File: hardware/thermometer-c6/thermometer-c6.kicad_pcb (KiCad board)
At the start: 2 copper layers, 48 x 35 mm, 101 parts, among them J1 JST-PH-2 BAT, J2 MEAS_HDR, J3 USB-C, J4 EPD FPC24 0.5mm, J5 DEBUG, Q1 AO3401A, Q2 AO3401A, Q3 Si1308EDL, Q4 AO3401A, Q5 2N7002, Q6 AO3401A, SW1 RESET, SW2 BOOT, U1 ESP32-C6-MINI-1-N4, U2 RT9080-33GJ5, U3 USBLC6-2SC6, U4 MCP73831-2, U5 BMP581, U6 BMP585, Y1 32.768kHz FC-135

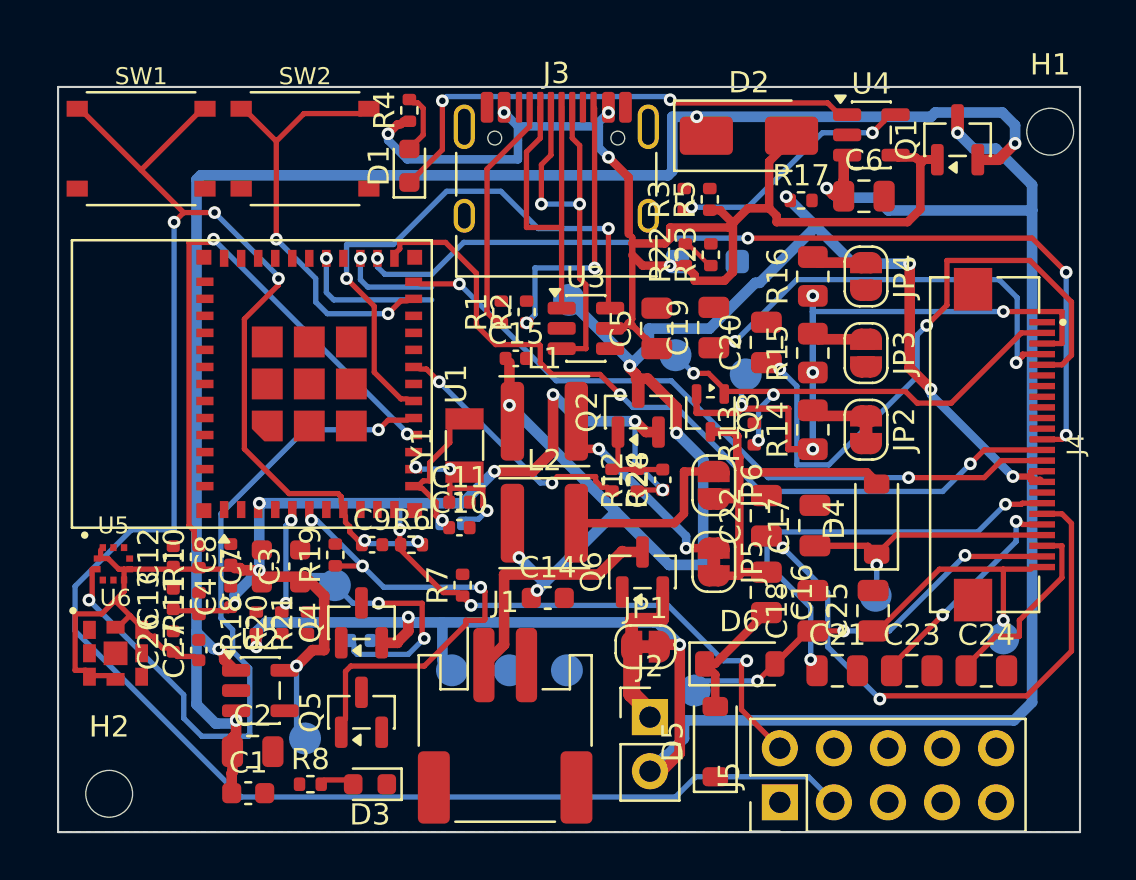
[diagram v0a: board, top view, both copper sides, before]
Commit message: Rebuild the divider block around its shared nodes; fence BOOT
R18/R20/R21 sat in one row at y25.17 with every shared node running
diagonally across it, and the row's north pads were 0.645mm from C3/C7's
(a 0.25mm lane needs 0.65). All four terminals starved.

Stack R20 over R21 instead, so VBAT_ADC is a 0.71mm link between adjacent
pads; R20 rot 180 puts ~VDIV_TOP straight across 1.77mm of clear copper
into Q4.3; R18 rot 270 drops ~VDIV_PGATE onto a lane under the ladder.
VBAT reaches R18.1 through a via-in-pad, so its 0.5mm B.Cu lane no longer
needs an F.Cu stub through the gate node's only escape. VBAT_ADC (50k
Thevenin) now runs 5mm to U1.5 through the C7/C3 pad channel instead of
the router's 15mm loop around the JST.

Box BOOT's A* to U1's north-east quadrant: with the divider unblocked it
reached R7.2 by running 60mm around the south edge and up the single
0.3mm B.Cu column between the antenna keep-out and the VSYS lane -- the
one corridor EN needs for SW1. R7.2 waits for R7 to move.

21 -> 17 unrouted terminals. DRC copper-clean.

Co-Authored-By: Claude Opus 4.8 (1M context) <noreply@anthropic.com>
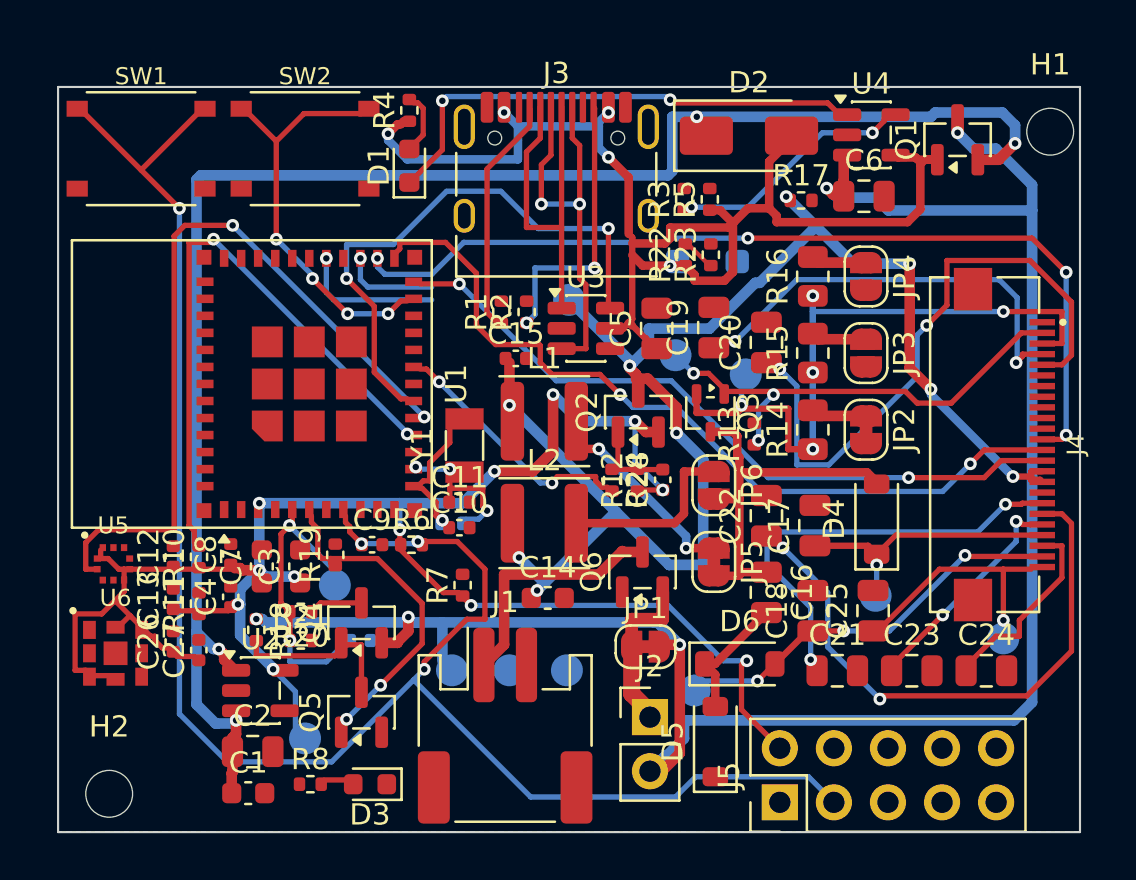
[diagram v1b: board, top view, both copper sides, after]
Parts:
- moved R20 1.03 mm to (111.4, 124.7), turned to 180 degrees
- moved R21 0.89 mm to (111.4, 126.0), turned to 0 degrees
- moved R18 0.33 mm to (109.3, 125.5), turned to -90 degrees
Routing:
- net EN: track 96.9 -> 84.6 mm, vias 5 -> 4
- net Net-(Q4-G): track 0.00 -> 8.36 mm
- net VDIV_EN: track 22.0 -> 14.9 mm, vias 3 -> 2
- net VBAT_ADC: track 17.1 -> 14.5 mm, vias 4 -> 2
- net Net-(Q4-D): track 0.00 -> 2.51 mm
- net SCL: track 34.1 -> 35.8 mm
- net +3V3: track 93.7 -> 92.0 mm, vias 11 -> 12
- net VBAT: track 96.0 -> 94.6 mm
- net BOOT: track 19.5 -> 18.9 mm, vias 2 -> 4

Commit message: Author J4's digital fan-out; route EPD_VCC before the signals
Pins 9..14 escape west at the connector's 0.5mm pitch and spread to 0.7mm,
the pitch a 0.6mm via needs beside a neighbouring lane. The six drops
cascade from the south, each in its own x-window: two parallel 45-degree
legs 0.5mm apart are only 0.354mm apart perpendicular, so no lane may be
diagonal beside a diagonal. The vias land in a staircase, not the usual
two columns -- each lane has to clear EPD_VCC's 45-degree B.Cu feed
(x-y = 26.55) before it can dive, and nothing here runs parallel to it.

EPD_VCC moves ahead of those six in ROUTE_PLAN. Q2.3's only escape is
north -- its own gate and source pads wall the south -- into the same B.Cu
channel over TP8 that the digital lanes cross the booster on. Routed after
them it lost Q2.3 and TP5.1 outright, and authoring around them cost four
HV escapes. Ordered first it takes a short F.Cu run through the y13.4
channel instead of the 20mm B.Cu loop it used to make.

Drop three pieces of authored copper the router now bypasses: EPD_CS and
EPD_DC's east-going stubs off U1's north row (both leave through their
via-in-pads instead, and the stubs walled the flank), EPD_DC's fan lane
(it escapes J4.11 eastward round the north edge) and EPD_SCK's staircase
via (it reaches the lane on F.Cu).

21 -> 15 unrouted terminals; EPD_MOSI/SCK/CS/DC and DBG_TX land. DRC
copper-clean; the remaining dangling copper is EPD_RST's and EPD_BUSY's,
and goes away when they route.

Co-Authored-By: Claude Opus 4.8 (1M context) <noreply@anthropic.com>
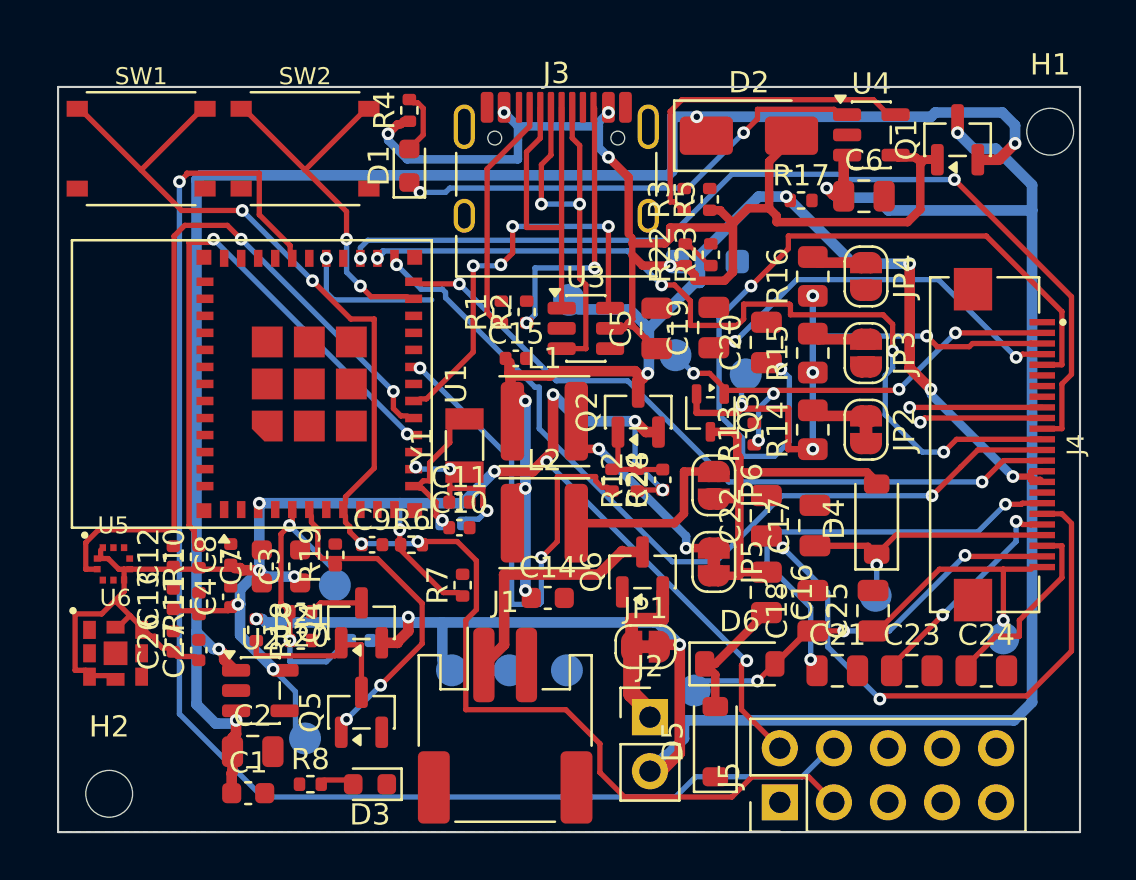
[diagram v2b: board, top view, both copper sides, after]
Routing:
- net DBG_TX: track 0.00 -> 65.9 mm, vias 0 -> 1
- net EPD_DC: track 4.49 -> 44.5 mm, vias 1 -> 2
- net EN: track 84.6 -> 65.2 mm
- net EPD_VCC: track 69.5 -> 55.4 mm, vias 9 -> 8
- net EPD_PWR_EN: track 11.5 -> 23.2 mm
- net USB_D-: track 26.2 -> 19.0 mm, vias 2 -> 4
- net Net-(J4-Pin_5): track 28.5 -> 35.6 mm
- net EPD_BUSY: track 6.69 -> 12.9 mm, vias 1 -> 2
- net EPD_RST: track 0.00 -> 5.81 mm, vias 0 -> 1
- net Net-(U4-PROG): track 11.0 -> 15.3 mm, vias 2 -> 0
- net EPD_RESE: track 30.3 -> 27.2 mm
- net BOOT: track 18.9 -> 16.4 mm, vias 4 -> 2
- net Net-(J4-Pin_4): track 19.2 -> 17.1 mm
- net EPD_SCK: track 37.7 -> 39.6 mm
- net EPD_CS: track 42.6 -> 40.8 mm
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
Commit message: Author J5's fan-in; keep the router's vias out of other holes
VBAT's 0.5mm B.Cu lane at y29.75 walls J5's entire north approach and
leaves 0.21mm of it clear of the pin rows. J5 is through-hole, so each
lane now surfaces on a via just north of that lane and drops onto the pads
on F.Cu, straight over it. The two outer-row pins come down the 0.84mm
channels between the inner pads, 0.295mm to each pad at 0.25mm width. The
five vias share one row at 1.27mm pitch.

route.py placed a via dead centre in J5.4's plated hole. build_bitmaps
stamps obstacles with *copper* clearance, and copper clearance is waived
against your own net -- so a same-net PTH pad reads as free space to drop a
via into. Hole-to-hole spacing has no such exemption. Stamp every drilled
pad and every via into the via bitmaps net-agnostically.

Still 15 unrouted, but the four debug lines and VBUS_SENSE now fail on
U1's side rather than J5's: the connector end is solved and the bus across
the board is what is left. DRC copper-clean. DBG_TX reaches J5.4 the long
way round the south edge for now, so its drop dangles until the bus lands.

Co-Authored-By: Claude Opus 4.8 (1M context) <noreply@anthropic.com>
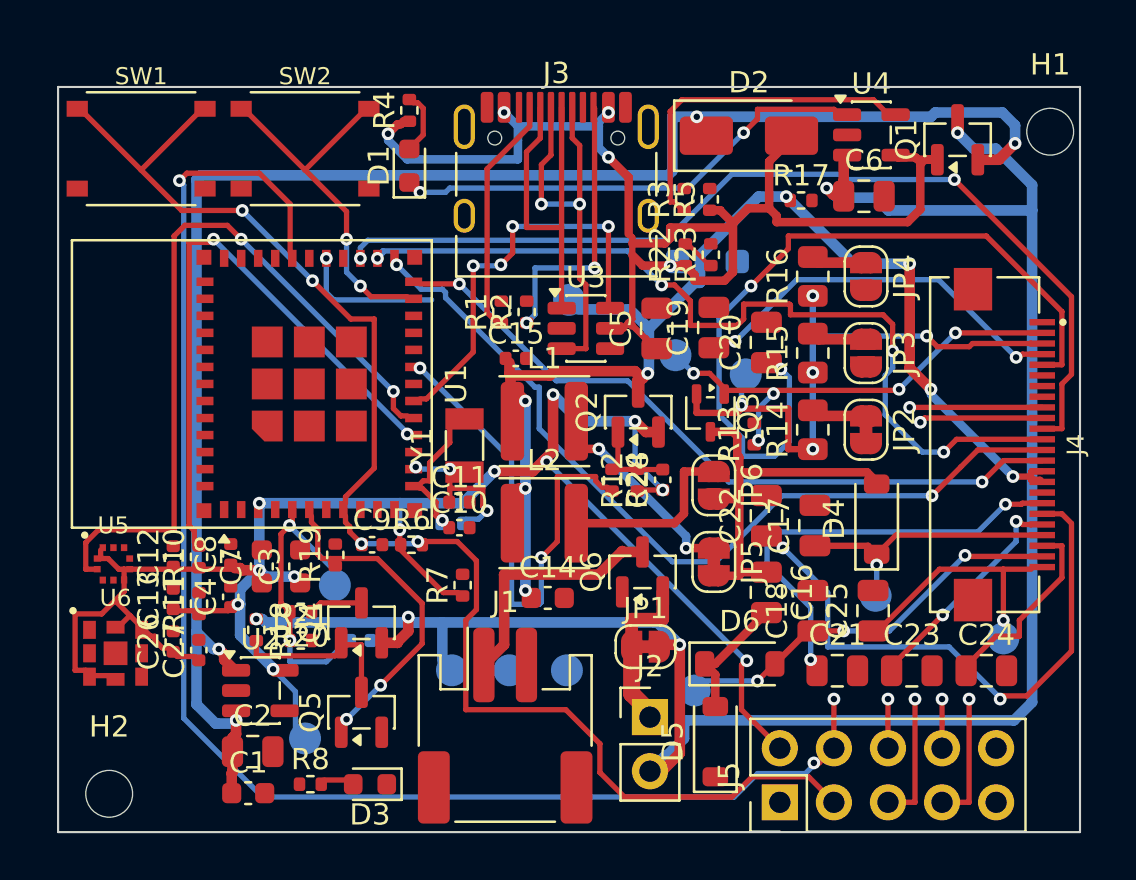
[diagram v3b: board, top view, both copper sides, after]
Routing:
- net DBG_RX: track 0.00 -> 6.12 mm, vias 0 -> 1
- net DBG_IO5: track 0.00 -> 6.12 mm, vias 0 -> 1
- net DBG_TX: track 65.9 -> 68.9 mm, vias 1 -> 3
- net VBUS_SENSE: track 1.79 -> 4.10 mm, vias 0 -> 1
- net DBG_IO8: track 0.00 -> 2.31 mm, vias 0 -> 1
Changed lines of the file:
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@@
 	)
 	(segment
-		(start 105.7 104.45)
-		(end 106.05 104.1)
+		(start 105.7 104.4)
+		(end 105.9 104.6)
 		(width 0.25)
-		(layer "F.Cu")
+		(layer "B.Cu")
 		(net "DBG_TX")
 	)
 	(segment
-		(start 105.7 129.449999)
-		(end 105.7 104.45)
+		(start 105.8 105.8)
+		(end 108.65 105.8)
 		(width 0.25)
-		(layer "B.Cu")
-		(net "DBG_TX")
+		(layer "F.Cu")
+		(net "EN")
 	)
 	(segment
-		(start 105.7 129.45)
-		(end 105.7 129.449999)
+		(start 105.9 104.6)
+		(end 105.9 129.65)
 		(width 0.25)
 		(layer "B.Cu")
@@
 	)
 	(segment
-		(start 105.8 105.8)
-		(end 108.65 105.8)
+		(start 105.9 129.65)
+		(end 109.6 133.35)
 		(width 0.25)
-		(layer "F.Cu")
-		(net "EN")
+		(layer "B.Cu")
+		(net "DBG_TX")
 	)
 	(segment
@@
 	(segment
 		(start 106.05 104.05)
-		(end 109.45 104.05)
-		(width 0.25)
-		(layer "F.Cu")
-		(net "DBG_TX")
-	)
-	(segment
-		(start 106.05 104.1)
-		(end 106.05 104.05)
+		(end 105.7 104.4)
 		(width 0.25)
 		(layer "F.Cu")
@@
 	(segment
 		(start 109.45 104.05)
-		(end 109.45 106)
-		(width 0.25)
-		(layer "F.Cu")
-		(net "DBG_TX")
-	)
-	(segment
-		(start 109.45 106)
-		(end 110.9 107.45)
+		(end 106.05 104.05)
 		(width 0.25)
 		(layer "F.Cu")
@@
 	(segment
 		(start 109.6 133.35)
-		(end 105.7 129.45)
+		(end 131.75 133.35)
 		(width 0.25)
 		(layer "B.Cu")
@@
 	)
 	(segment
-		(start 110.9 107.45)
-		(end 110.9 107.75)
+		(start 110.9 105.5)
+		(end 109.45 104.05)
+		(width 0.25)
+		(layer "F.Cu")
+		(net "DBG_TX")
+	)
+	(segment
+		(start 110.9 107.75)
+		(end 110.9 105.5)
 		(width 0.25)
 		(layer "F.Cu")
@@
 	)
 	(segment
-		(start 129 133.349999)
-		(end 129 133.35)
-		(width 0.25)
-		(layer "B.Cu")
-		(net "DBG_TX")
-	)
-	(segment
-		(start 129 133.35)
-		(end 109.6 133.35)
-		(width 0.25)
-		(layer "B.Cu")
-		(net "DBG_TX")
-	)
-	(segment
 		(start 129.199999 105.65)
 		(end 128.949999 105.4)
@@
 	)
 	(segment
-		(start 129.949999 132.4)
-		(end 129 133.349999)
-		(width 0.25)
-		(layer "B.Cu")
-		(net "DBG_TX")
-	)
-	(segment
 		(start 129.989999 114.4225)
 		(end 129.99 114.422501)
@@
 	)
 	(segment
+		(start 131.75 133.35)
+		(end 132.85 132.25)
+		(width 0.25)
+		(layer "B.Cu")
+		(net "DBG_TX")
+	)
+	(segment
 		(start 131.8 111.95)
 		(end 134.7 109.05)
@@
 	)
 	(segment
+		(start 132.85 132.25)
+		(end 135.1 132.25)
+		(width 0.25)
+		(layer "B.Cu")
+		(net "DBG_TX")
+	)
+	(segment
 		(start 132.9 105.15)
 		(end 134.199999 105.15)
@@
 	)
 	(segment
-		(start 134.95 132.4)
-		(end 129.949999 132.4)
+		(start 135.1 132.25)
+		(end 135.5 131.85)
 		(width 0.25)
 		(layer "B.Cu")
@@
 	)
 	(segment
+		(start 135.5 131.75)
+		(end 135.75 131.75)
+		(width 0.25)
+		(layer "F.Cu")
+		(net "DBG_TX")
+	)
+	(segment
+		(start 135.5 131.85)
+		(end 135.5 131.75)
+		(width 0.25)
+		(layer "B.Cu")
+		(net "DBG_TX")
+	)
+	(segment
 		(start 135.7125 108.25)
 		(end 137.95 108.25)
@@
 	)
 	(segment
-		(start 135.8 131.55)
-		(end 134.95 132.4)
-		(width 0.25)
-		(layer "B.Cu")
-		(net "DBG_TX")
-	)
-	(segment
-		(start 135.95 131.55)
-		(end 135.8 131.55)
+		(start 135.75 131.75)
+		(end 136.44 131.06)
 		(width 0.25)
-		(layer "B.Cu")
+		(layer "F.Cu")
 		(net "DBG_TX")
 	)
@@
 	(segment
 		(start 136.15 126.3)
-		(end 138.6 128.75)
+		(end 141.85 126.3)
 		(width 0.25)
 		(layer "B.Cu")
@@
 	)
 	(segment
+		(start 136.44 128.75)
+		(end 136.44 131.06)
+		(width 0.25)
+		(layer "F.Cu")
+		(net "DBG_TX")
+	)
+	(segment
+		(start 136.44 131.06)
+		(end 136.45 131.05)
+		(width 0.25)
+		(layer "F.Cu")
+		(net "DBG_TX")
+	)
+	(segment
 		(start 136.45 101.05)
 		(end 136.5 101.1)
@@
 	)
 	(segment
-		(start 138.6 128.75)
-		(end 138.75 128.6)
-		(width 0.25)
-		(layer "F.Cu")
-		(net "Net-(J4-Pin_19)")
-	)
-	(segment
 		(start 138.75 110.7)
 		(end 139.2 111.15)
@@
 	)
 	(segment
-		(start 138.75 128.6)
-		(end 145.5 128.6)
-		(width 0.25)
-		(layer "F.Cu")
-		(net "Net-(J4-Pin_19)")
-	)
-	(segment
 		(start 138.8 125.25)
 		(end 141.4 122.65)
@@
 	)
 	(segment
+		(start 138.98 128.75)
+		(end 138.98 131.06)
+		(width 0.25)
+		(layer "F.Cu")
+		(net "VBUS_SENSE")
+	)
+	(segment
 		(start 139 105.8)
 		(end 138.4 105.2)
@@
 	)
 	(segment
+		(start 140.25 128.75)
+		(end 140.25 133.6)
+		(width 0.25)
+		(layer "F.Cu")
+		(net "DBG_RX")
+	)
+	(segment
+		(start 140.25 133.6)
+		(end 138.98 133.6)
+		(width 0.25)
+		(layer "F.Cu")
+		(net "DBG_RX")
+	)
+	(segment
 		(start 140.28 103.31)
 		(end 140.3875 103.4175)
@@
 	)
 	(segment
+		(start 141.52 128.75)
+		(end 141.52 131.06)
+		(width 0.25)
+		(layer "F.Cu")
+		(net "DBG_IO8")
+	)
+	(segment
 		(start 141.55 124.8)
 		(end 145 121.35)
@@
 	)
 	(segment
+		(start 141.85 126.3)
+		(end 144.249999 128.699999)
+		(width 0.25)
+		(layer "B.Cu")
+		(net "Net-(J4-Pin_19)")
+	)
+	(segment
 		(start 142.1 104.35)
 		(end 137 104.35)
@@
 	)
 	(segment
+		(start 142.79 128.75)
+		(end 142.79 133.6)
+		(width 0.25)
+		(layer "F.Cu")
+		(net "DBG_IO5")
+	)
+	(segment
+		(start 142.79 133.6)
+		(end 141.52 133.6)
+		(width 0.25)
+		(layer "F.Cu")
+		(net "DBG_IO5")
+	)
+	(segment
 		(start 142.8 112.2)
 		(end 141.3 112.2)
@@
 	)
 	(segment
+		(start 144.249999 128.699999)
+		(end 144.25 128.699999)
+		(width 0.25)
+		(layer "B.Cu")
+		(net "Net-(J4-Pin_19)")
+	)
+	(segment
+		(start 144.25 128.699999)
+		(end 144.25 128.75)
+		(width 0.25)
+		(layer "B.Cu")
+		(net "Net-(J4-Pin_19)")
+	)
+	(segment
+		(start 144.25 128.75)
+		(end 144.4 128.6)
+		(width 0.25)
+		(layer "F.Cu")
+		(net "Net-(J4-Pin_19)")
+	)
+	(segment
 		(start 144.35 101.2)
 		(end 144.95 101.8)
@@
 	)
 	(segment
+		(start 144.4 128.6)
+		(end 145.5 128.6)
+		(width 0.25)
+		(layer "F.Cu")
+		(net "Net-(J4-Pin_19)")
+	)
+	(segment
 		(start 144.5 119.6)
 		(end 145.25 119.6)
@@
 	)
 	(via
-		(at 105.7 104.45)
+		(at 105.7 104.4)
 		(size 0.6)
 		(drill 0.3)
@@
 	)
 	(via
+		(at 135.5 131.75)
+		(size 0.6)
+		(drill 0.3)
+		(layers "F.Cu" "B.Cu")
+		(net "DBG_TX")
+	)
+	(via
 		(at 136.1 104.75)
 		(size 0.6)
@@
 	)
 	(via
+		(at 136.44 128.75)
+		(size 0.6)
+		(drill 0.3)
+		(layers "F.Cu" "B.Cu")
+		(net "DBG_TX")
+	)
+	(via
 		(at 136.9 125.55)
 		(size 0.6)
@@
 	)
 	(via
-		(at 138.6 128.75)
+		(at 138.98 128.75)
 		(size 0.6)
 		(drill 0.3)
 		(layers "F.Cu" "B.Cu")
-		(net "Net-(J4-Pin_19)")
+		(net "VBUS_SENSE")
 	)
 	(via
@@
 	)
 	(via
+		(at 140.25 128.75)
+		(size 0.6)
+		(drill 0.3)
+		(layers "F.Cu" "B.Cu")
+		(net "DBG_RX")
+	)
+	(via
 		(at 140.5 115.75)
 		(size 0.6)
@@
 	)
 	(via
+		(at 141.52 128.75)
+		(size 0.6)
+		(drill 0.3)
+		(layers "F.Cu" "B.Cu")
+		(net "DBG_IO8")
+	)
+	(via
 		(at 141.55 124.8)
 		(size 0.6)
@@
 	)
 	(via
+		(at 142.79 128.75)
+		(size 0.6)
+		(drill 0.3)
+		(layers "F.Cu" "B.Cu")
+		(net "DBG_IO5")
+	)
+	(via
 		(at 143.4 118.55)
 		(size 0.6)
@@
 	)
 	(via
+		(at 144.25 128.75)
+		(size 0.6)
+		(drill 0.3)
+		(layers "F.Cu" "B.Cu")
+		(net "Net-(J4-Pin_19)")
+	)
+	(via
